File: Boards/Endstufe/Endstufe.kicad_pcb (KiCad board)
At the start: 2 copper layers, 153 x 111 mm, 62 parts, among them J1 HV In, J2 Relais, J3 NF_In, J4 Trafo, K1 G6E, P4 6V3_AC, P6 6V3_DC, P8 Bias, T1 KT88, T2 KT88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

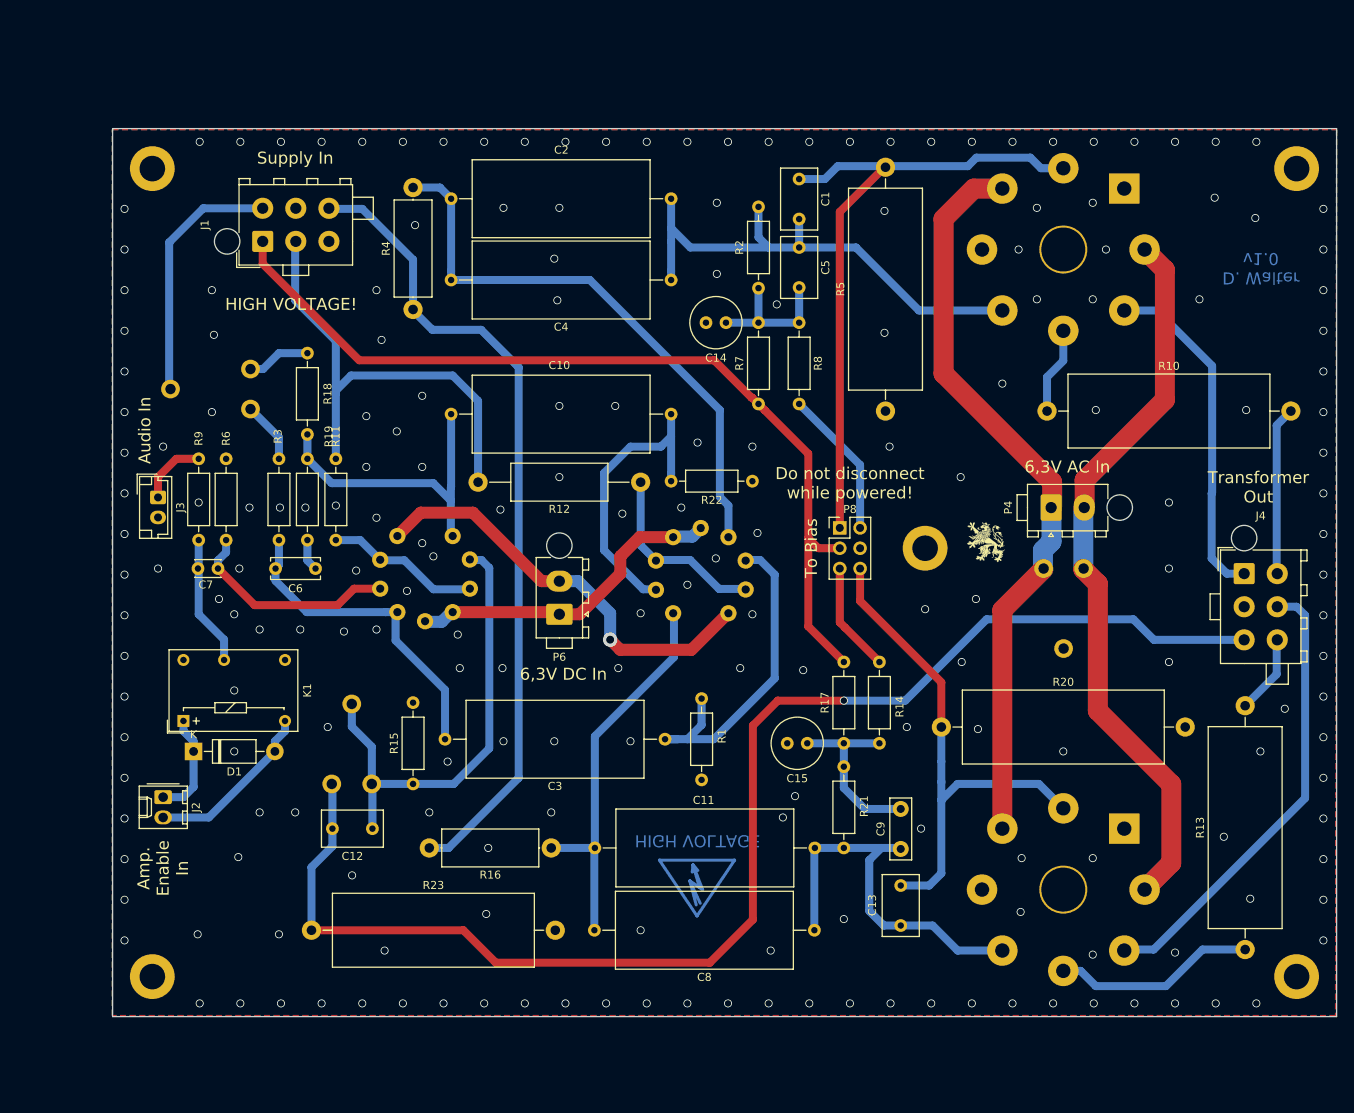
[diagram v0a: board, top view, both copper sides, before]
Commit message: Reworked Delay + Layout changed
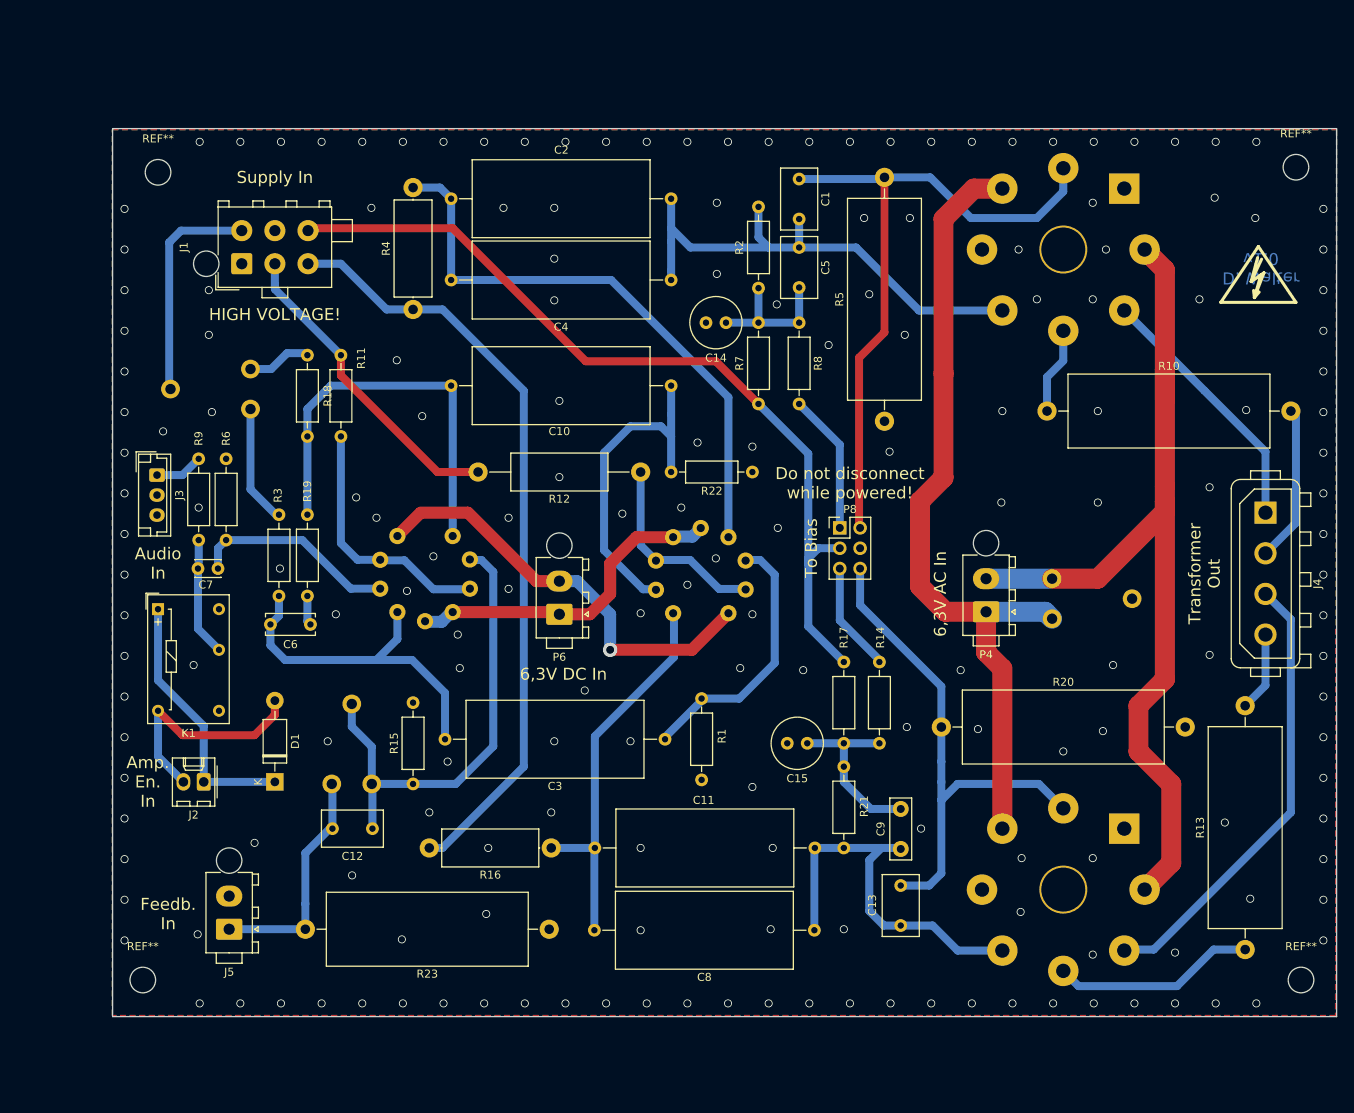
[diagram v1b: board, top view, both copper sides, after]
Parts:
- removed G*** (x2): LOGO, Loewe:Loewe_Klein
- removed the REF** at (63.9, 56.2)
- removed the REF** at (63.9, 157.2)
- removed the REF** at (207.0, 157.2)
- removed the REF** at (207.0, 56.2)
- removed the REF** at (160.5, 103.6)
- removed the REF** at (132.0, 145.4)
- added J5: Gegenkopplung, Connector_TE-Connectivity:TE_MATE-N-LOK_1-770866-x_1x02_P4.14mm_Vertical, F.Cu at (73.5, 151.3)
- added REF**: Symbol_HighVoltage_Type2_SilkTop_VerySmall, Loewe:Symbol_HighVoltage_Type2_SilkTop_VerySmall, B.Cu at (133.1, 146.8)
- added REF**: Symbol_HighVoltage_Type2_SilkTop_VerySmall, Loewe:Symbol_HighVoltage_Type2_SilkTop_VerySmall, F.Cu at (202.2, 70.1)
- added REF**: MountingHole_3.2mm_M3, MountingHole:MountingHole_3.2mm_M3, F.Cu at (64.6, 56.6)
- added REF**: MountingHole_3.2mm_M3, MountingHole:MountingHole_3.2mm_M3, F.Cu at (206.9, 56.0)
- added REF**: MountingHole_3.2mm_M3, MountingHole:MountingHole_3.2mm_M3, F.Cu at (207.5, 157.6)
- added REF**: MountingHole_3.2mm_M3, MountingHole:MountingHole_3.2mm_M3, F.Cu at (62.7, 157.6)
- J3: value NF_In -> Audio_In; footprint Connector_JST:JST_EH_B2B-EH-A_1x02_P2.50mm_Vertical -> Connector_JST:JST_EH_B3B-EH-A_1x03_P2.50mm_Vertical
- J4: value Trafo -> Übertrager; footprint Connector_TE-Connectivity:TE_MATE-N-LOK_1-770875-x_2x03_P4.14mm_Vertical -> Connector_TE-Connectivity:TE_MATE-N-LOK_350211-1_1x04_P5.08mm_Vertical
- moved P4 15.4 mm to (168.1, 111.6), turned to 180 degrees
- moved K1 14.3 mm to (64.6, 111.3), turned to 0 degrees
- moved R11 13.0 mm to (87.5, 89.7)
- moved D1 10.9 mm to (79.2, 132.8), turned to 90 degrees
- moved J4 8.07 mm to (203.1, 99.2), turned to 270 degrees
- moved C6 7.01 mm to (83.7, 113.2)
- moved R19 6.98 mm to (83.3, 99.4)
- moved R3 6.98 mm to (79.8, 99.4)
- moved J2 5.43 mm to (70.4, 132.8), turned to 180 degrees
- moved RV3 4.14 mm to (176.4, 107.4), turned to 0 degrees
- moved J1 3.83 mm to (75.1, 68.1)
- moved C10 3.56 mm to (128.8, 83.3)
- moved J3 2.80 mm to (64.5, 94.5)
- moved R5 1.28 mm to (155.4, 87.8)
- moved R12 1.27 mm to (125.0, 94.1)
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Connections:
- net Net-(J4-Pad1) renamed /+450V_T1
- J1 pad 1: -60V -> GND
- J1 pad 3: GND -> +300V
- J1 pad 6: +300V -> -60V
- J4 pad 2: GND -> Net-(J4-Pad2)
- J4 pad 3: Net-(C12-Pad2) -> /+450V_T2
- K1 pad 12: (no net) -> GND
- P8 pad 1: Bias_1 -> UG_1
- P8 pad 2: UG_1 -> Bias_1
- R10 pad 2: Net-(J4-Pad4) -> Net-(J4-Pad2)
- R13 pad 2: Net-(J4-Pad6) -> Net-(J4-Pad4)
- T2 pad 3: Net-(J4-Pad5) -> /+450V_T2
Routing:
- net Net-(C12-Pad2): track 170.8 -> 29.3 mm, vias 1 -> 0
- net Net-(J4-Pad5): track 57.3 -> 0.00 mm
- net /+450V_T2: track 0.00 -> 56.6 mm
- net Net-(P4-Pad2): track 91.2 -> 116.4 mm
- net -120V: track 59.4 -> 39.5 mm
- net Net-(D1-Pad1): track 13.1 -> 32.8 mm
- net Net-(J4-Pad2): track 0.00 -> 19.6 mm
- net Net-(C10-Pad2): track 38.5 -> 51.3 mm
- net Net-(R11-Pad1): track 19.1 -> 31.6 mm
- net Net-(J4-Pad4): track 21.1 -> 9.94 mm
- net /+450V_T1: track 42.9 -> 32.7 mm
- net Net-(J4-Pad6): track 9.89 -> 0.00 mm
- net Net-(P4-Pad1): track 93.4 -> 102.2 mm
- net Net-(C3-Pad1): track 41.5 -> 33.3 mm
- net Net-(R3-Pad1): track 7.70 -> 14.9 mm
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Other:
- board text added: "Amp. En. In"
- board text added: "Feedb. In"
- board text removed: "Amp. Enable In"
- board text removed: "HIGH VOLTAGE"

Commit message: Work in progess - many LAyour changes
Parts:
- removed P4: 6V3_AC, Connector_TE-Connectivity:TE_MATE-N-LOK_1-770866-x_1x02_P4.14mm_Vertical
- removed P8: Bias, Connector_PinHeader_2.54mm:PinHeader_2x03_P2.54mm_Vertical
- removed RV3: 500R, Potentiometer_THT:Potentiometer_Piher_PT-10-V10_Vertical
- added G***: LOGO, Loewe:Loewe_Klein, F.Cu at (53.3, 53.3)
- added G***: LOGO, Loewe:Loewe_Klein, B.Cu at (66.0, 108.7)
- added J10: 240V VU, Connector_TE-Connectivity:TE_MATE-N-LOK_1-770866-x_1x02_P4.14mm_Vertical, F.Cu at (73.7, 51.3)
- added J6: 12V out, Connector_Molex:Molex_KK-254_AE-6410-02A_1x02_P2.54mm_Vertical, F.Cu at (53.3, 130.3)
- added J7: Conn_01x08, Connector_PinHeader_2.54mm:PinHeader_2x04_P2.54mm_Vertical, F.Cu at (152.3, 101.0)
- added J8: 12V In, Connector_Molex:Molex_KK-254_AE-6410-02A_1x02_P2.54mm_Vertical, F.Cu at (53.3, 141.8)
- added J9: VU-Meter, Connector_TE-Connectivity:TE_MATE-N-LOK_1-770866-x_1x02_P4.14mm_Vertical, F.Cu at (186.7, 99.2)
- added P1: 6V3_AC, Connector_TE-Connectivity:TE_MATE-N-LOK_1-770866-x_1x02_P4.14mm_Vertical, F.Cu at (160.0, 43.7)
- added P2: 6V3_AC, Connector_TE-Connectivity:TE_MATE-N-LOK_1-770866-x_1x02_P4.14mm_Vertical, F.Cu at (181.6, 130.3)
- C14, C15: value 10µF / 100V -> 10µF/100V; footprint Capacitor_THT:C_Radial_D6.3mm_H5.0mm_P2.50mm -> Capacitor_THT:CP_Radial_D6.3mm_P2.50mm
- C6: footprint Capacitor_THT:C_Disc_D6.0mm_W2.5mm_P5.00mm -> Capacitor_THT:C_Disc_D6.0mm_W4.4mm_P5.00mm
- C7: footprint Capacitor_THT:C_Disc_D3.0mm_W2.0mm_P2.50mm -> Capacitor_THT:C_Axial_L22.0mm_D9.5mm_P27.50mm_Horizontal
- C9: footprint Capacitor_THT:C_Disc_D7.5mm_W2.5mm_P5.00mm -> Capacitor_THT:C_Disc_D7.5mm_W4.4mm_P5.00mm
- R10, R13, R20, R23, R5: footprint Resistor_THT:R_Axial_Power_L25.0mm_W9.0mm_P30.48mm -> Resistor_THT:R_Axial_DIN0922_L20.0mm_D9.0mm_P25.40mm_Horizontal
- R11: value 68k -> 68k/1W; footprint Resistor_THT:R_Axial_DIN0207_L6.3mm_D2.5mm_P10.16mm_Horizontal -> Resistor_THT:R_Axial_DIN0207_L6.3mm_D2.5mm_P15.24mm_Horizontal
- R12: footprint Resistor_THT:R_Axial_DIN0414_L11.9mm_D4.5mm_P20.32mm_Horizontal -> Resistor_THT:R_Axial_DIN0207_L6.3mm_D2.5mm_P15.24mm_Horizontal
- R16, R4: footprint Resistor_THT:R_Axial_DIN0414_L11.9mm_D4.5mm_P15.24mm_Horizontal -> Resistor_THT:R_Axial_DIN0207_L6.3mm_D2.5mm_P10.16mm_Horizontal
- RV2, RV5: footprint Potentiometer_THT:Potentiometer_Piher_PT-10-V10_Vertical -> Potentiometer_THT:Potentiometer_Piher_PT-10-V10_Vertical_Hole; moved to F.Cu
- moved REF** 131.8 mm to (70.6, 62.8)
- moved J2 65.1 mm to (53.3, 70.0), turned to 270 degrees
- moved D1 55.7 mm to (65.4, 78.9), turned to 180 degrees
- moved R6 44.8 mm to (66.0, 136.7), turned to 90 degrees
- moved R5 34.7 mm to (189.8, 83.4), turned to 180 degrees
- moved K1 27.6 mm to (66.6, 83.7), turned to 270 degrees
- moved REF** 25.8 mm to (107.3, 145.6), turned to 90 degrees
- moved R9 25.3 mm to (58.4, 115.1), turned to 90 degrees
- moved R10 23.1 mm to (198.9, 85.9), turned to 90 degrees
- moved J3 22.3 mm to (51.4, 112.5), turned to 90 degrees
- moved R4 20.6 mm to (113.6, 62.4)
- moved J1 19.9 mm to (90.4, 55.4)
- moved REF** 19.6 mm to (51.9, 41.7)
- moved C2 18.6 mm to (145.7, 52.2)
- moved C4 17.9 mm to (145.7, 64.3)
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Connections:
- RV2 pad 1: Net-(R3-Pad1) -> Net-(R18-Pad2)
- RV2 pad 3: Net-(R18-Pad2) -> Net-(R3-Pad1)
- RV5 pad 2: Net-(C12-Pad1) -> Net-(C12-Pad2)
- T1 pad 2: Net-(P4-Pad2) -> Net-(P1-Pad1)
- T1 pad 7: Net-(P4-Pad1) -> Net-(P1-Pad2)
- T2 pad 2: Net-(P4-Pad2) -> Net-(P2-Pad1)
- T2 pad 7: Net-(P4-Pad1) -> Net-(P2-Pad2)
- U1 pad 4: Net-(P6-Pad1) -> Net-(P6-Pad2)
- U1 pad 5: Net-(P6-Pad1) -> Net-(P6-Pad2)
- U1 pad 9: Net-(P6-Pad2) -> Net-(P6-Pad1)
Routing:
- net +12V: track 0.00 -> 184.2 mm
- net Net-(P4-Pad2): track 116.4 -> 0.00 mm
- net Net-(P4-Pad1): track 102.2 -> 0.00 mm
- net Net-(P1-Pad1): track 0.00 -> 50.2 mm
- net Net-(J4-Pad2): track 19.6 -> 51.7 mm
- net Net-(P2-Pad1): track 0.00 -> 28.8 mm
- net /+450V_T1: track 32.7 -> 61.2 mm
- net Net-(C1-Pad2): track 65.0 -> 40.9 mm
- net -60V: track 107.5 -> 124.6 mm
- net Net-(R10-Pad1): track 10.9 -> 28.0 mm
- net Net-(D1-Pad2): track 28.9 -> 12.5 mm
- net Net-(P2-Pad2): track 0.00 -> 16.3 mm
- net Net-(C12-Pad2): track 29.3 -> 45.5 mm
- net -120V: track 39.5 -> 53.2 mm
- net +240V: track 28.1 -> 41.3 mm
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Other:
- board size 153 x 111 mm -> 165 x 130 mm
- board text added: "+"
- board text added: "12V In/Out"
- board text added: "240V Out"
- board text added: "Driver Sym. Adjust"
- board text added: "HIGH VOLTAGE! Do not Touch Board when powered!"
- board text added: "VU-Meter out"
- board text removed: "Driver Bias Adjust"
- board text removed: "KT88 Heater Adjust"

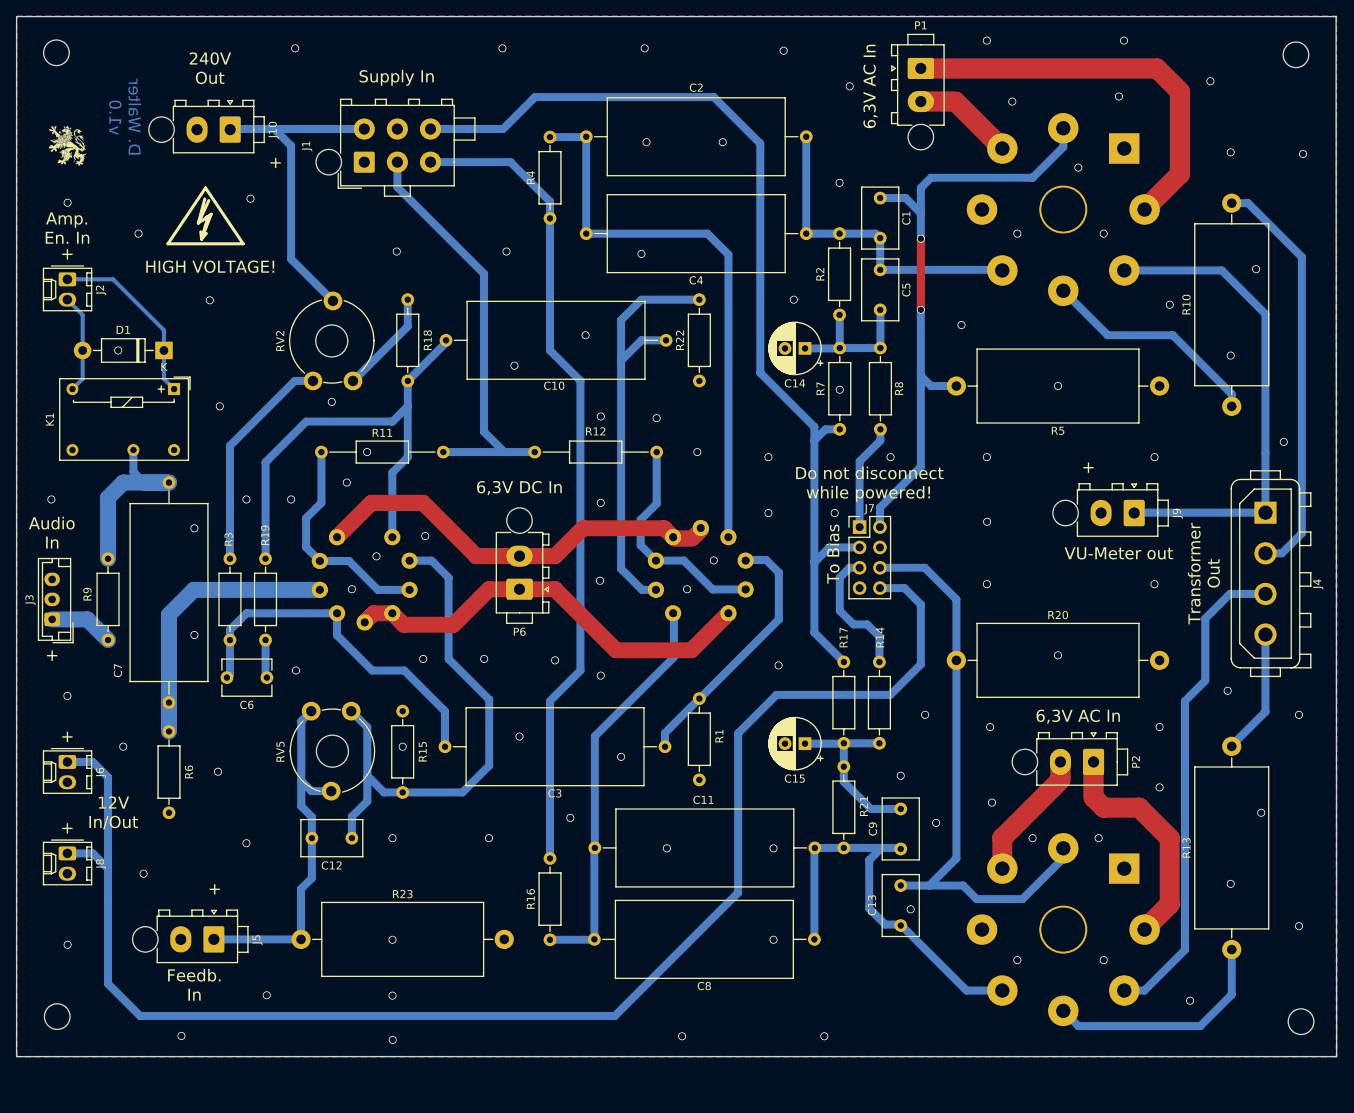
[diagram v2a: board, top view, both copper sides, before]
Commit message: 6.3V, 400V und 400V Regler Boards bestellt
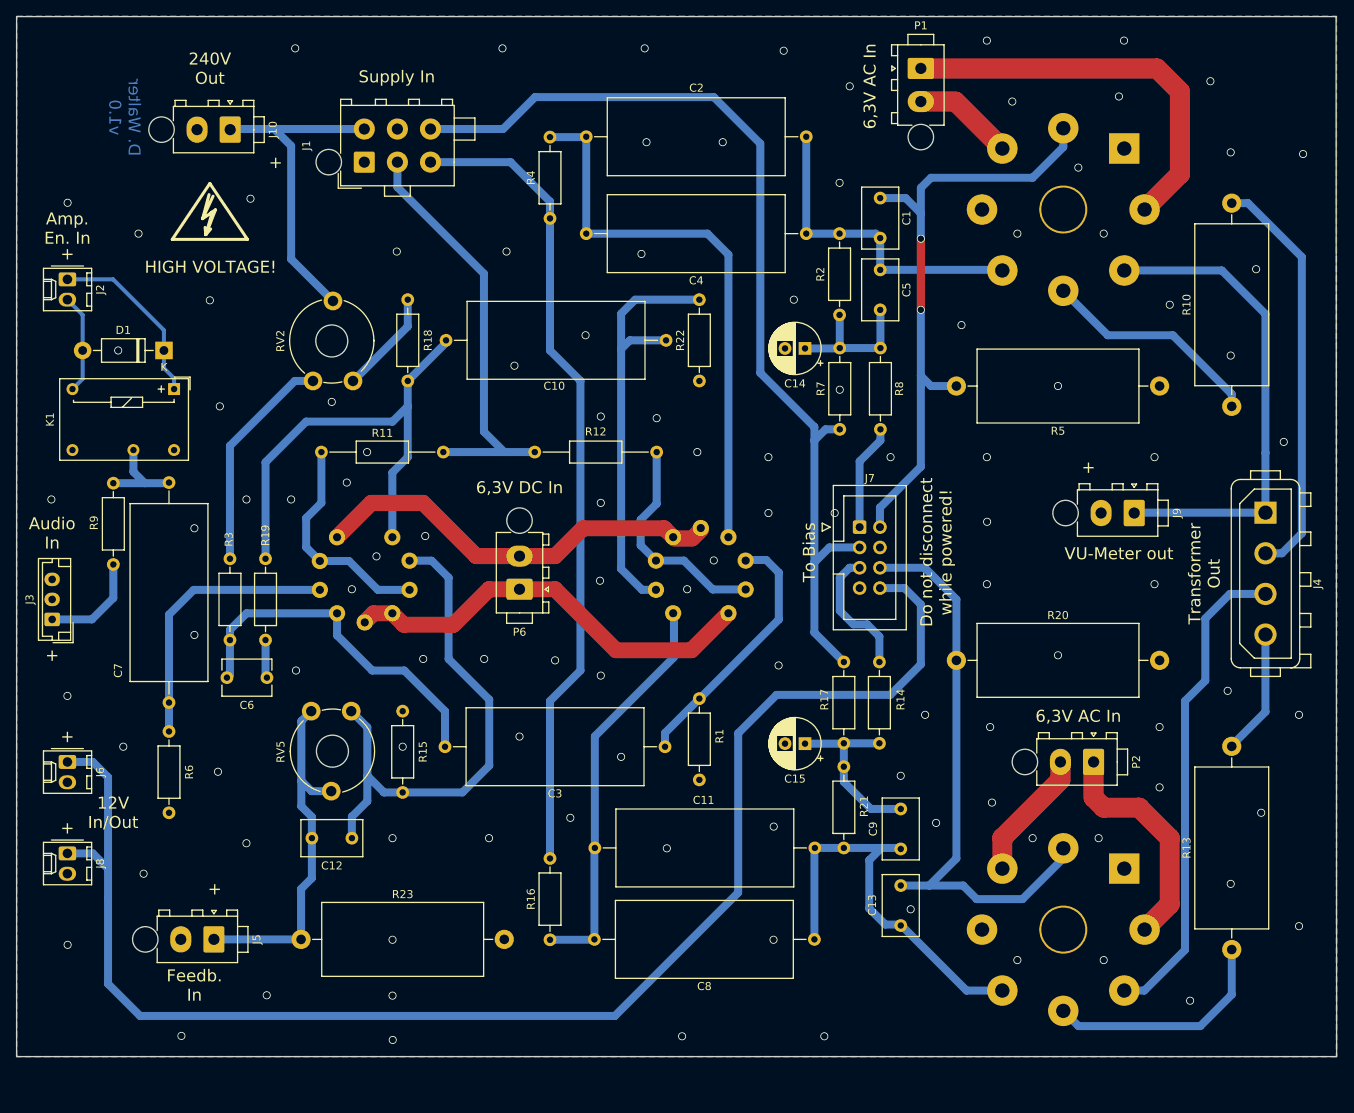
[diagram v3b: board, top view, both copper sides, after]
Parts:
- removed the G*** at (53.3, 53.3)
- removed the G*** at (66.0, 108.7)
- removed the REF** at (107.3, 145.6)
- removed the REF** at (70.6, 62.8)
- removed the REF** at (51.9, 41.7)
- removed the REF** at (206.9, 42.0)
- removed the REF** at (207.5, 162.8)
- removed the REF** at (52.0, 162.2)
- added G***: LOGO, Loewe:Loewe_Klein, B.Cu at (53.0, 50.3)
- added G***: LOGO, Loewe:HV, B.Cu at (139.1, 146.1)
- added REF**: Symbol_HighVoltage_Type2_SilkTop_VerySmall, Loewe:Symbol_HighVoltage_Type2_SilkTop_VerySmall, F.Cu at (71.1, 62.2)
- J7: footprint Connector_PinHeader_2.54mm:PinHeader_2x04_P2.54mm_Vertical -> Connector_IDC:IDC-Header_2x04_P2.54mm_Vertical
- moved R9 19.6 mm to (59.1, 95.5), turned to -90 degrees
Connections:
- R9 pad 1: Net-(J3-Pad1) -> Net-(C7-Pad1)
- R9 pad 2: Net-(C7-Pad1) -> Net-(J3-Pad1)
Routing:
- net Net-(C7-Pad1): track 23.8 -> 11.7 mm
- net Net-(J3-Pad1): track 8.05 -> 12.9 mm
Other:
- net class Default removed
- net class HV removed
- net class Heizung removed
- net class Signal removed
